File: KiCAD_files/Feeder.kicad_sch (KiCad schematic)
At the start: 82 parts, among them J405 Conn_01x02_Male, J406 Conn_01x02_Male, J501 Conn_01x03, Q501 60V N channel, Q502 TK13P25D,RQ, T501 PA2467NL, U407 OPA316, U501 NCP12700, U503 TL431MFDT,215

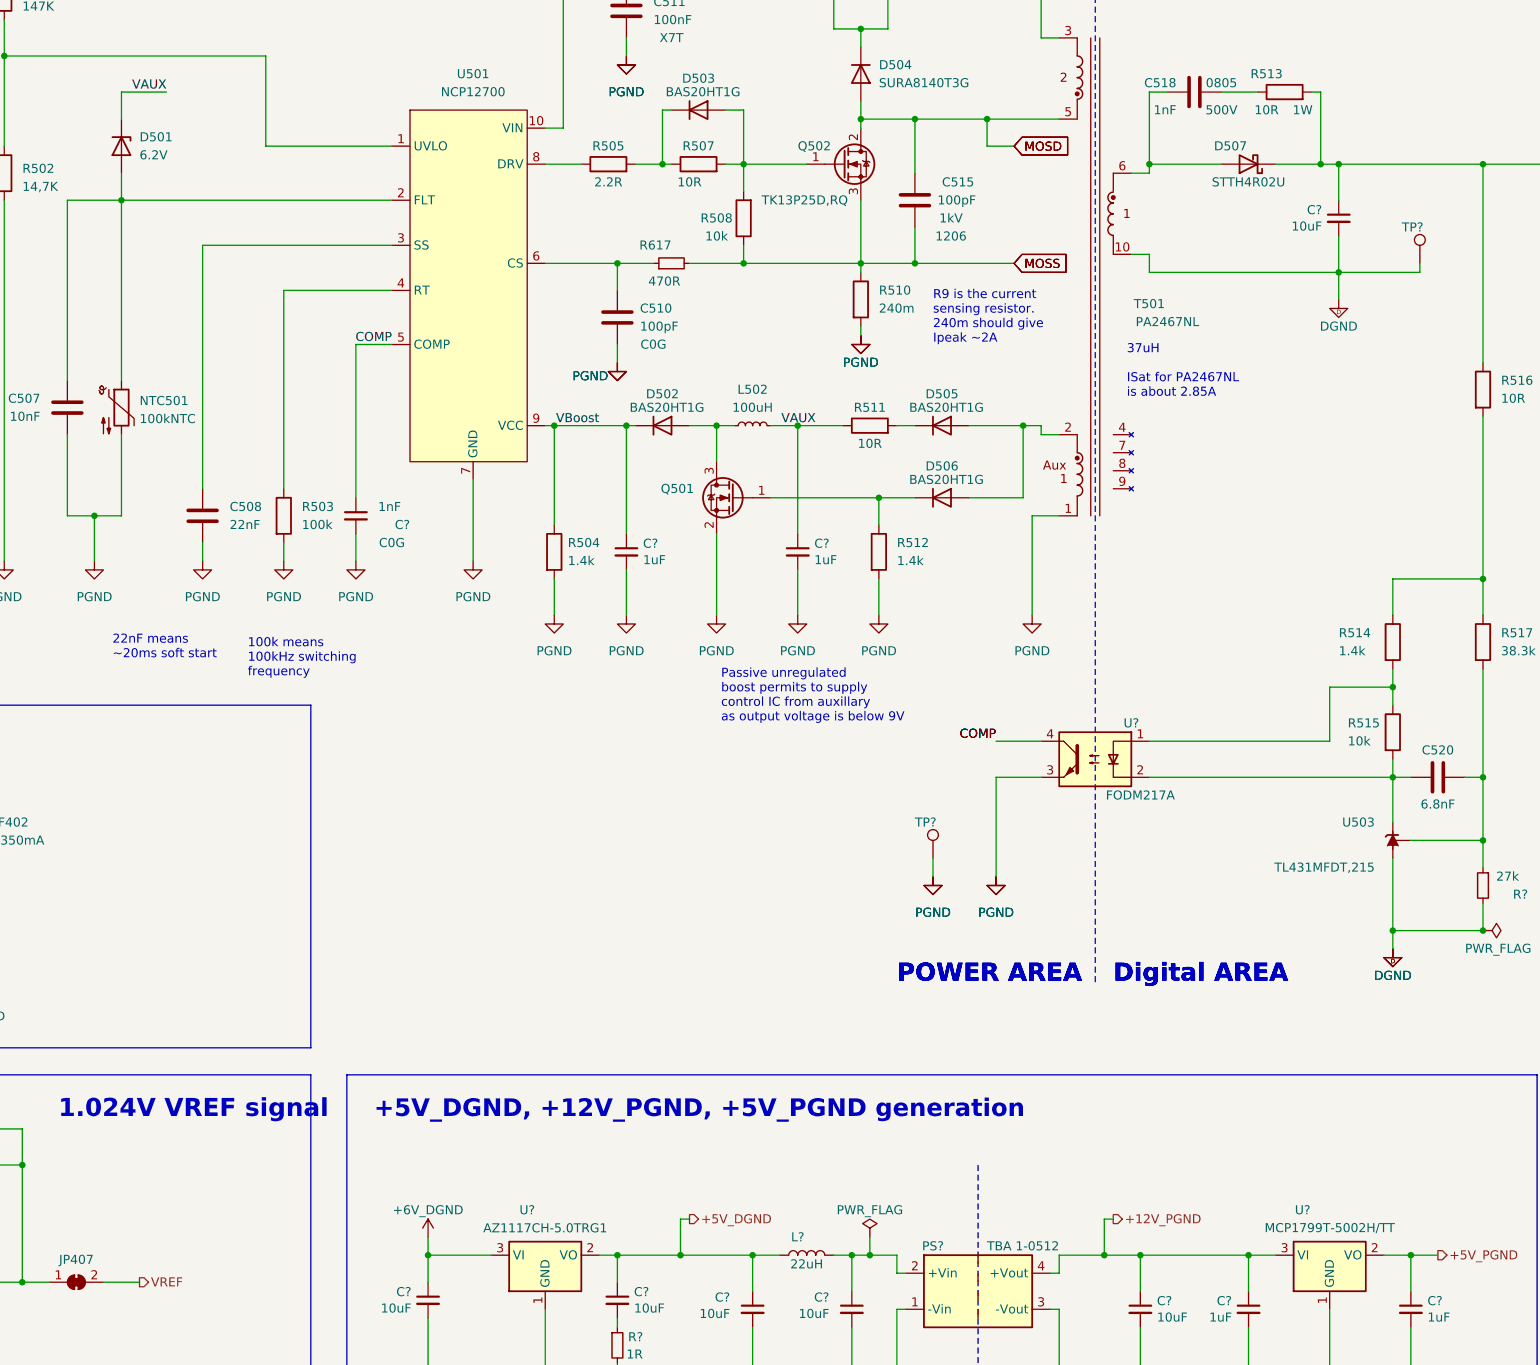
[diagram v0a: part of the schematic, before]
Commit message: Schematic freeze before PCB modifications
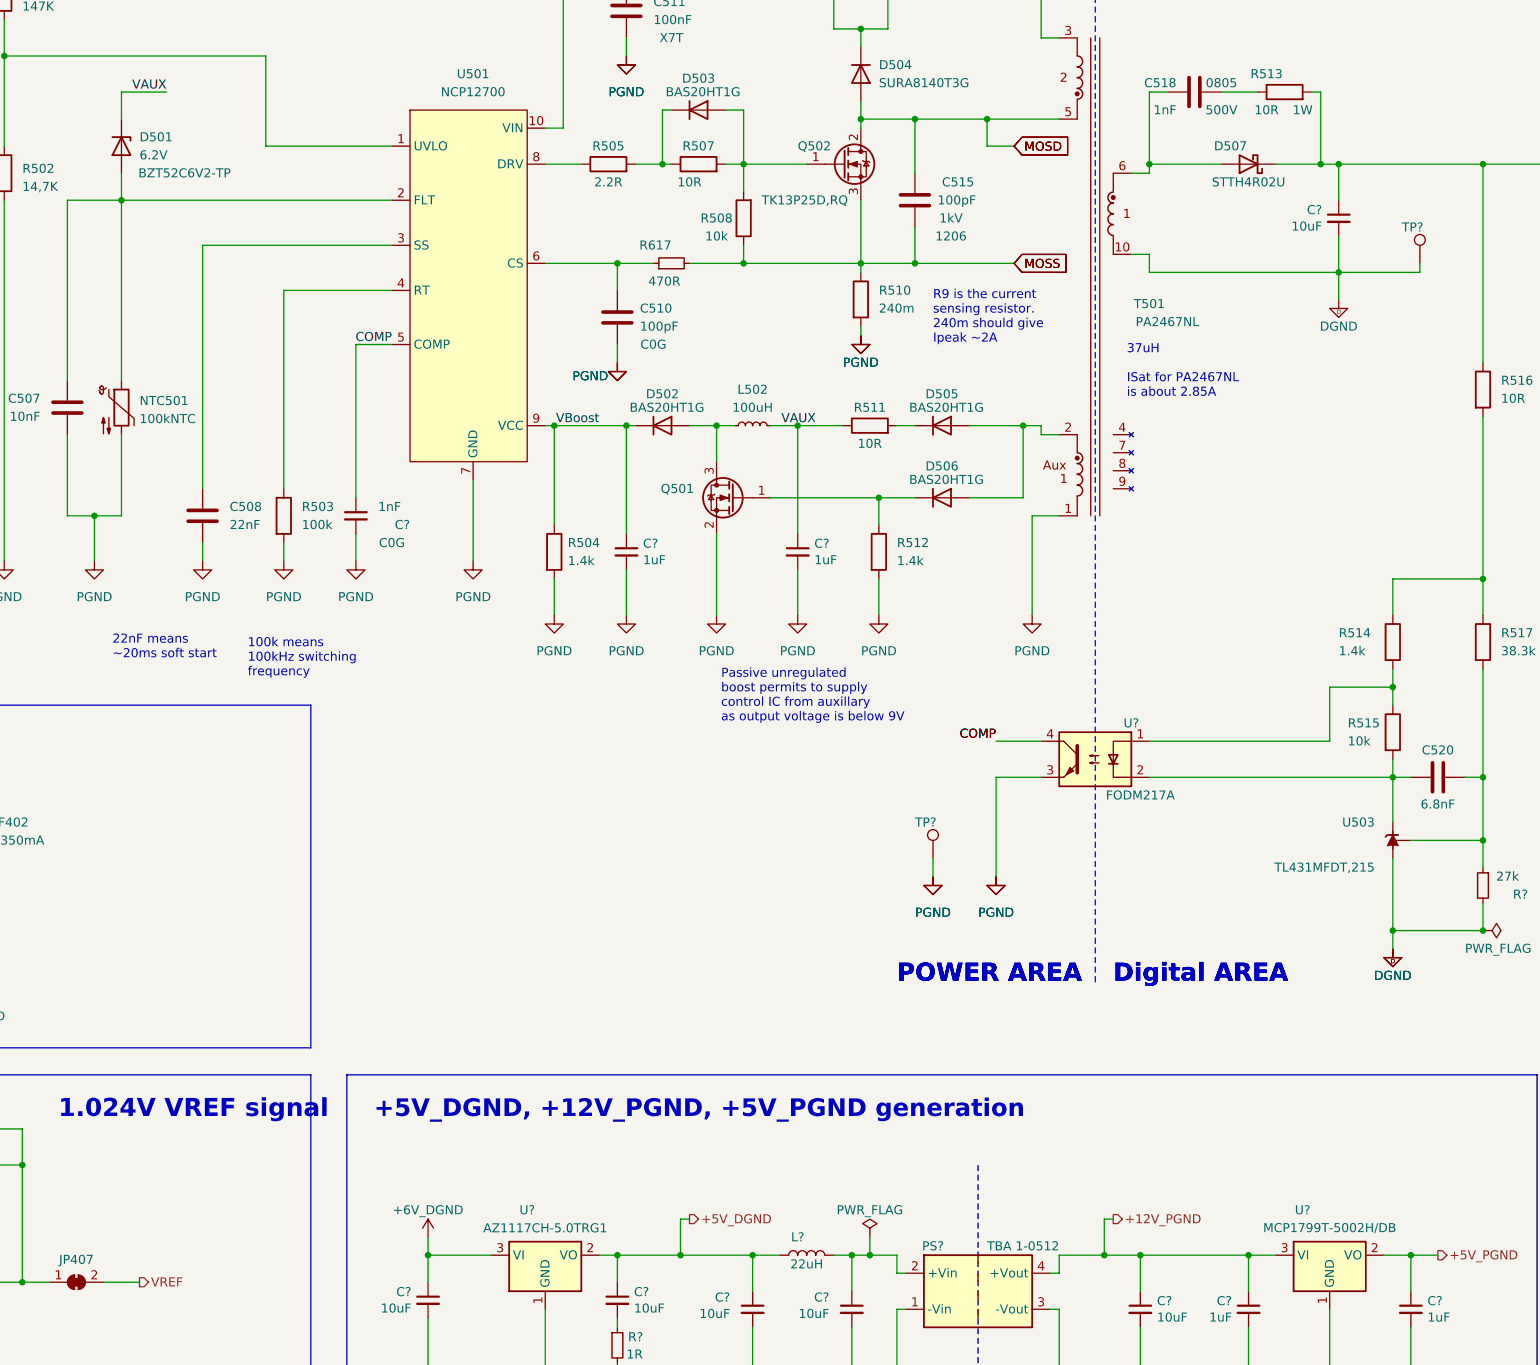
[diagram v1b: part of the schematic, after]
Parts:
- D501: footprint Diode_SMD:D_SOD-323_HandSoldering -> Footprints:D_SOD-123
- U407: footprint Package_TO_SOT_SMD:SOT-353_SC-70-5 -> Package_TO_SOT_SMD:SOT-353_SC-70-5_Handsoldering
- U?: value MCP1799T-5002H/TT -> MCP1799T-5002H/DB; footprint Footprints:SOT-23_copy -> Package_TO_SOT_SMD:SOT-223; manf# MCP1799T-5002H/TT -> MCP1799T-5002H/DB
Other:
- title: OWNVERTER V0.1 -> OWNVERTER V1.0
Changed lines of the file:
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@@
   (paper "A3")
   (title_block
-    (title "OWNVERTER V0.1")
+    (title "OWNVERTER V1.0")
     (comment 1 "TWR")
   )
@@
       (effects (font (size 1.27 1.27)) (justify left) hide)
     )
-    (property "Datasheet" "https://power.murata.com/pub/data/power/ncl/kdc_mee1.pdf" (at 241.3 256.54 0)
+    (property "Datasheet" "https://www.tracopower.com/sites/default/files/products/datasheets/tba1_datasheet.pdf" (at 241.3 256.54 0)
       (effects (font (size 1.27 1.27)) (justify left) hide)
     )
@@
       (effects (font (size 1.27 1.27)) hide)
     )
-    (property "Manf#" "" (at 77.47 66.04 0)
-      (effects (font (size 1.27 1.27)) hide)
-    )
     (property "Ref" "ok" (at 77.47 66.04 0)
       (effects (font (size 1.27 1.27)) hide)
@@
       (effects (font (size 1.27 1.27)) hide)
     )
-    (property "Datasheet" "https://www.vishay.com/docs/20019/rcwe.pdf" (at 198.12 109.22 0)
+    (property "Datasheet" "~" (at 198.12 109.22 0)
       (effects (font (size 1.27 1.27)) hide)
     )
@@
       (effects (font (size 1.27 1.27)))
     )
-    (property "Value" "MCP1799T-5002H/TT" (at 264.16 240.0046 0)
+    (property "Value" "MCP1799T-5002H/DB" (at 264.16 240.0046 0)
       (effects (font (size 1.27 1.27)))
     )
-    (property "Footprint" "Footprints:SOT-23_copy" (at 264.16 238.125 0)
+    (property "Footprint" "Package_TO_SOT_SMD:SOT-223" (at 264.16 238.125 0)
       (effects (font (size 1.27 1.27)) hide)
     )
-    (property "Datasheet" "http://ww1.microchip.com/downloads/en/DeviceDoc/20002276C.pdf" (at 264.16 243.84 0)
+    (property "Datasheet" "https://www.mouser.fr/datasheet/2/268/MCP1799_Data_Sheet_20006248B-2887414.pdf" (at 264.16 243.84 0)
       (effects (font (size 1.27 1.27)) hide)
     )
@@
       (effects (font (size 1.27 1.27)) hide)
     )
-    (property "manf#" "MCP1799T-5002H/TT" (at 264.16 243.84 0)
+    (property "manf#" "MCP1799T-5002H/DB" (at 264.16 243.84 0)
       (effects (font (size 1.27 1.27)) hide)
     )
@@
       (effects (font (size 1.27 1.27)) hide)
     )
-    (property "Datasheet" "http://www.vishay.com/docs/83740/sfh617a.pdf" (at 240.03 166.37 0)
+    (property "Datasheet" "https://www.onsemi.com/download/data-sheet/pdf/fodm214-d.pdf" (at 240.03 166.37 0)
       (effects (font (size 1.27 1.27)) hide)
     )
@@
   )
   (symbol (lib_id "Device:D_Zener") (at 93.98 87.63 270) (unit 1)
-    (in_bom yes) (on_board yes) (dnp no) (fields_autoplaced)
-    (property "Reference" "D501" (at 96.52 86.3599 90)
+    (in_bom yes) (on_board yes) (dnp no)
+    (property "Reference" "D501" (at 96.52 86.36 90)
       (effects (font (size 1.27 1.27)) (justify left))
     )
@@
       (effects (font (size 1.27 1.27)) (justify left))
     )
-    (property "Footprint" "Diode_SMD:D_SOD-323_HandSoldering" (at 93.98 87.63 0)
+    (property "Footprint" "Footprints:D_SOD-123" (at 93.98 87.63 0)
       (effects (font (size 1.27 1.27)) hide)
     )
-    (property "Datasheet" "https://www.mouser.fr/datasheet/2/308/1/MM3Z2V4T1_D-2316321.pdf" (at 93.98 87.63 0)
+    (property "Datasheet" "https://www.mouser.fr/datasheet/2/258/BZT52C2V4_7eBZT52C75_500mW__SOD_123_-2510203.pdf" (at 93.98 87.63 0)
       (effects (font (size 1.27 1.27)) hide)
     )
-    (property "manf#" "BZT52C6V2-TP" (at 93.98 87.63 0)
-      (effects (font (size 1.27 1.27)) hide)
+    (property "manf#" "BZT52C6V2-TP" (at 102.87 91.44 90)
+      (effects (font (size 1.27 1.27)))
     )
     (pin "1")
@@
       (effects (font (size 1.27 1.27)) (justify left))
     )
-    (property "Footprint" "Package_TO_SOT_SMD:SOT-353_SC-70-5" (at 69.85 247.65 0)
+    (property "Footprint" "Package_TO_SOT_SMD:SOT-353_SC-70-5_Handsoldering" (at 69.85 247.65 0)
       (effects (font (size 1.27 1.27)) hide)
     )
-    (property "Datasheet" "http://www.ti.com/lit/ds/symlink/tlv6001.pdf" (at 64.77 247.65 0)
+    (property "Datasheet" "https://www.ti.com/lit/ds/symlink/opa316.pdf?ts=1683791438609&ref_url=https%253A%252F%252Fwww.google.com%252F" (at 64.77 247.65 0)
       (effects (font (size 1.27 1.27)) hide)
     )
